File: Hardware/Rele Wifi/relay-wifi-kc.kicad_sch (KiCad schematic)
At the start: 47 parts, among them J1 SalidaRele1, J2 SalidaRele2, J3 SalidaRele3, J4 SalidaRele4, K1 RELAY_C, K2 RELAY_C, K3 RELAY_C, K4 RELAY_C, Q1 TO23, Q2 TO23, Q3 TO23, Q4 TO23, U1 LM78M05_TO220, U2 ESP32_DevKit_V1_DOIT, U3 PC817, U4 PC817, U5 PC817, U6 PC817

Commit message: Esquematico y PCB V5
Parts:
- removed Q1, Q2, Q3, Q4: TO23, Package_TO_SOT_SMD:SOT-23, symbol Simulation_SPICE:NPN
- added I2C1: Conn_01x04, Connector_PinSocket_2.54mm:PinSocket_1x04_P2.54mm_Vertical, symbol Connector_Generic:Conn_01x04
- added Q1, Q2, Q3, Q5: BC817, Package_TO_SOT_SMD:SOT-23, symbol Transistor_BJT:BC817
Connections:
- net +5V: now also I2C1.1 (Pin_1)
- net GND: now also I2C1.4 (Pin_4)
- net at R9.1: now also Q3.2 (E)
- net at D12.2 (A), K4.5: now also Q3.3 (C)
- net at R5.1: now also Q3.1 (B)
- net at R6.1: now also Q1.2 (E)
- net at R2.1: now also Q1.1 (B)
- net at R8.1: now also Q5.2 (E)
- net at D8.2 (A), K2.5: now also Q5.3 (C)
- net at R3.1: now also Q5.1 (B)
- net at D6.2 (A), K1.5: now also Q1.3 (C)
- net GPIO18: now reaches U2.30 (IO18)
- net GPIO18: now also R12.1
- net GPIO19: now reaches U2.31 (IO19)
- net GPIO19: now also R13.1
- net GPIO21: now reaches U2.32 (IO21)
- net GPIO21: now also I2C1.2 (Pin_2)
- net GPIO22: now reaches U2.35 (IO22)
- net GPIO22: now also I2C1.3 (Pin_3)
- net at D10.2 (A), K3.5: now also Q2.3 (C)
- net at R4.1: now also Q2.1 (B)
- net at R7.1: now also Q2.2 (E)
- net GIPIO26: no longer names the net of U2.9 (IO26)
- net GIPIO26: no longer R11.1
- net GIPIO27: no longer names the net of U2.10 (IO27)
- net GIPIO27: no longer R10.1
- net GIPIO32 renamed GPIO32
- net GPIO32: now also R11.1; no longer R13.1
- net GIPIO33 renamed GPIO33
- net GPIO33: now also R10.1; no longer R12.1
- no-connect marks 30 -> 28
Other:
- moved on the sheet: U2

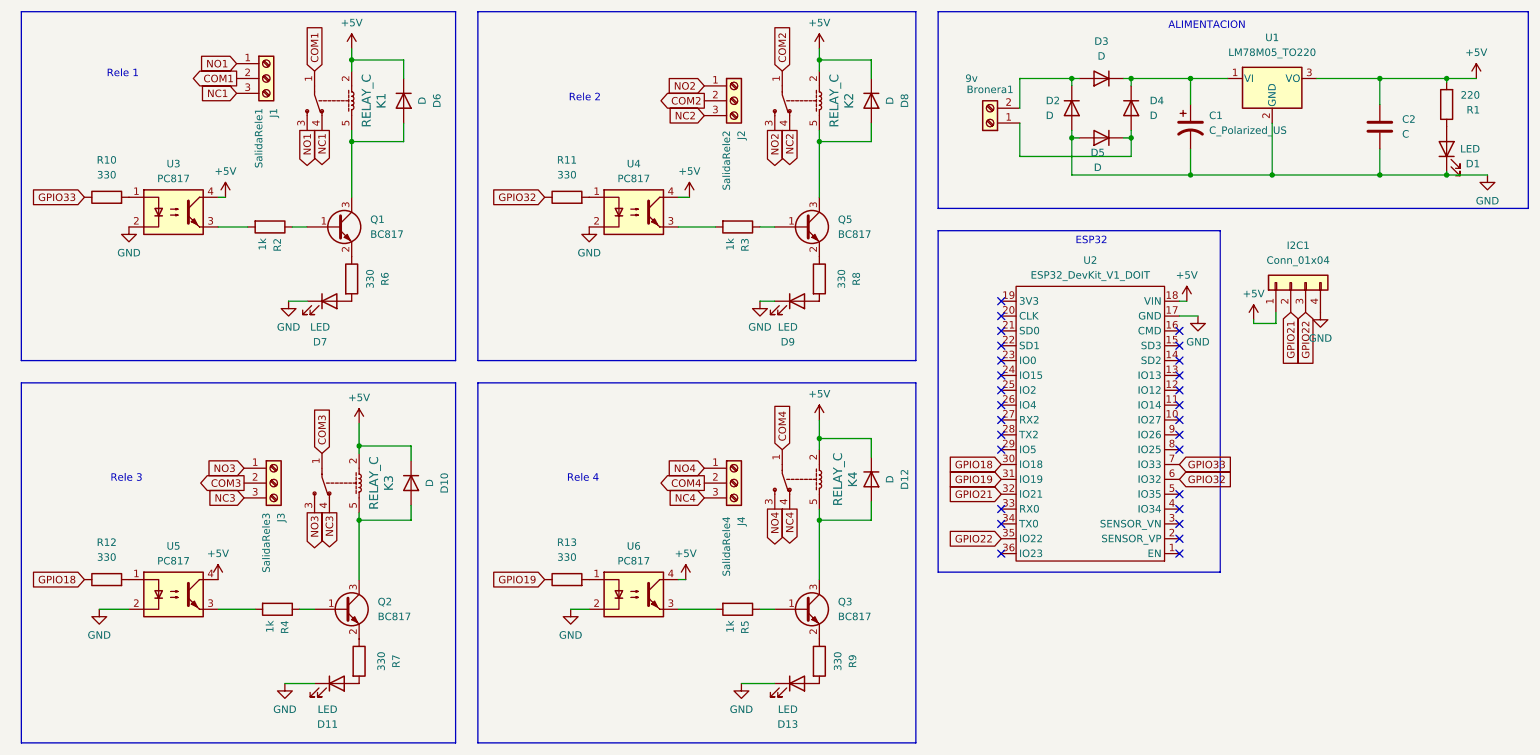
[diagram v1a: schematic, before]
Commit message: Esquematico y PCB V6
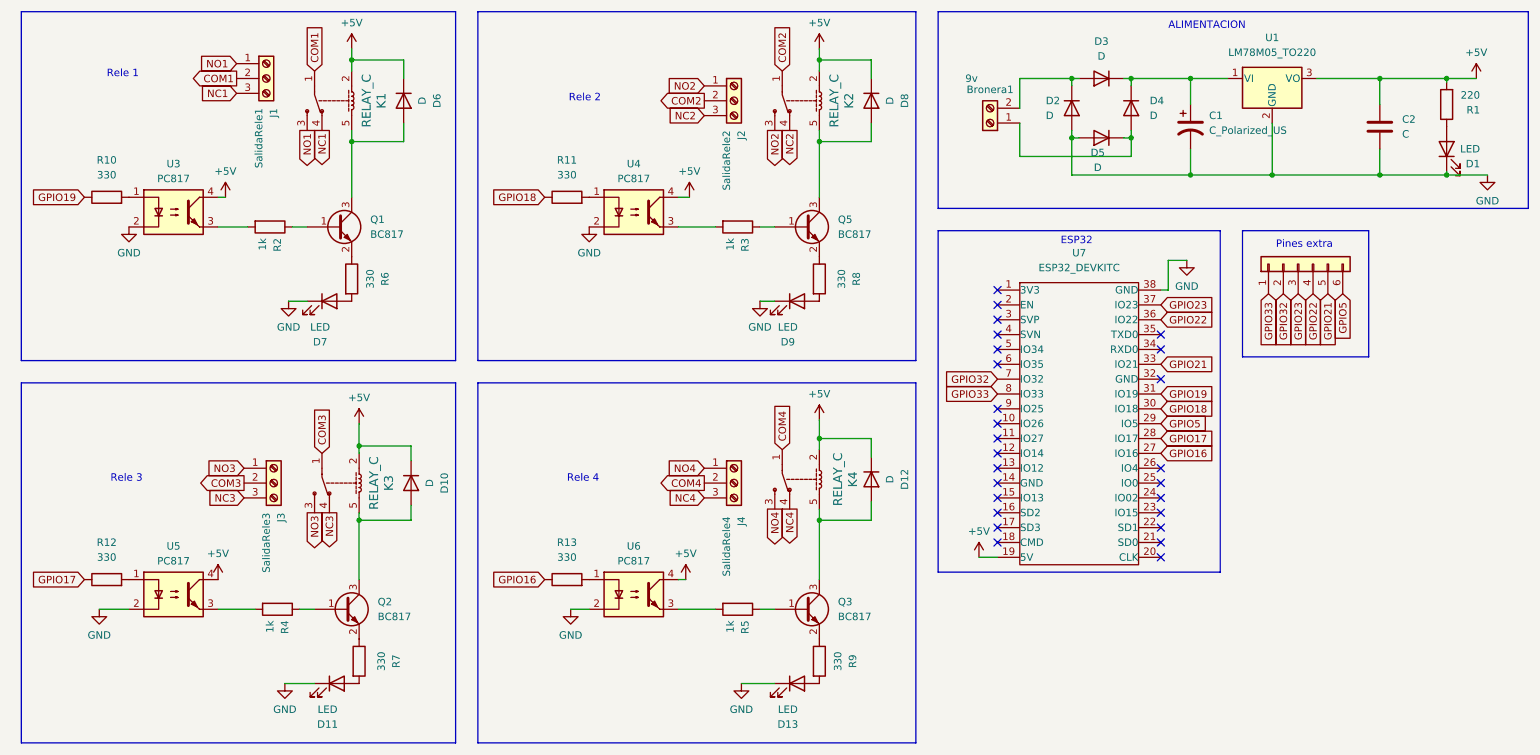
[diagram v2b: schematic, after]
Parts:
- removed I2C1: Conn_01x04, Connector_PinSocket_2.54mm:PinSocket_1x04_P2.54mm_Vertical, symbol Connector_Generic:Conn_01x04
- removed U2: ESP32_DevKit_V1_DOIT, EESTN5:ESP32_DEVKIT_V1_DOIT, symbol EESTN5:ESP32_DevKit_V1_DOIT
- added J5: Conn_01x06, Connector_PinSocket_2.54mm:PinSocket_1x06_P2.54mm_Vertical, symbol Connector_Generic:Conn_01x06
- added U7: ESP32_DEVKITC, EESTN5:ESP32S, symbol EESTN5:ESP32_DEVKITC
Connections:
- net +5V: now also U7.19 (5V)
- net GND: now also U7.38 (GND)
- net GPIO18: now also R11.1, U7.30 (IO18); no longer R12.1
- net GPIO19: now also R10.1, U7.31 (IO19); no longer R13.1
- net GPIO21: now also J5.5 (Pin_5), U7.33 (IO21)
- net GPIO22: now also J5.4 (Pin_4), U7.36 (IO22)
- net GPIO32: now also J5.2 (Pin_2), U7.7 (IO32); no longer R11.1
- net GPIO33: now also J5.1 (Pin_1), U7.8 (IO33); no longer R10.1
- new net GPIO16: R13.1, U7.27 (IO16)
- new net GPIO17: R12.1, U7.28 (IO17)
- new net GPIO23: J5.3 (Pin_3), U7.37 (IO23)
- new net GPIO5: J5.6 (Pin_6), U7.29 (IO5)
- no-connect marks 28 -> 26
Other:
- note added: "Pines extra"

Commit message: Esquematico y PCB V7
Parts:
- removed J5: Conn_01x06, Connector_PinSocket_2.54mm:PinSocket_1x06_P2.54mm_Vertical, symbol Connector_Generic:Conn_01x06
- added J5: Conn_01x10, Connector_PinSocket_2.54mm:PinSocket_1x10_P2.54mm_Vertical, symbol Connector_Generic:Conn_01x10
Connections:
- net GPIO21: now also J5.10 (Pin_10)
- net GPIO22: now also J5.9 (Pin_9)
- net GPIO32: now also J5.6 (Pin_6)
- net GPIO33: now also J5.5 (Pin_5)
- net GPIO26: now reaches U7.10 (IO26)
- net GPIO26: now also J5.3 (Pin_3)
- net GPIO27: now reaches U7.11 (IO27)
- net GPIO27: now also J5.2 (Pin_2)
- net GPIO13: now reaches U7.15 (IO13)
- net GPIO13: now also J5.1 (Pin_1)
- net GPIO34: now reaches U7.5 (IO34)
- net GPIO34: now also J5.8 (Pin_8)
- net GPIO35: now reaches U7.6 (IO35)
- net GPIO35: now also J5.7 (Pin_7)
- net GPIO25: now reaches U7.9 (IO25)
- net GPIO25: now also J5.4 (Pin_4)
- no-connect marks 26 -> 20

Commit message: Esquematico y PCB V8
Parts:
- D11, D13, D7, D9: footprint Connector_PinSocket_2.54mm:PinSocket_1x02_P2.54mm_Vertical -> TerminalBlock_Altech:Altech_AK300_1x02_P5.00mm_45-Degree
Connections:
- net +5V: now also R6.1, R7.1, R8.1, R9.1
- net GND: now also Q1.2 (E), Q2.2 (E), Q3.2 (E), Q5.2 (E); no longer D11.1 (K), D13.1 (K), D7.1 (K), D9.1 (K)
- net at D12.2 (A), K4.5, Q3.3 (C): now also D13.1 (K)
- net at D6.2 (A), K1.5, Q1.3 (C): now also D7.1 (K)
- net at D8.2 (A), K2.5, Q5.3 (C): now also D9.1 (K)
- net at D10.2 (A), K3.5, Q2.3 (C): now also D11.1 (K)
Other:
- moved on the sheet: D13, R9
